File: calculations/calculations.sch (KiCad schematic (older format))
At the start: 24 parts

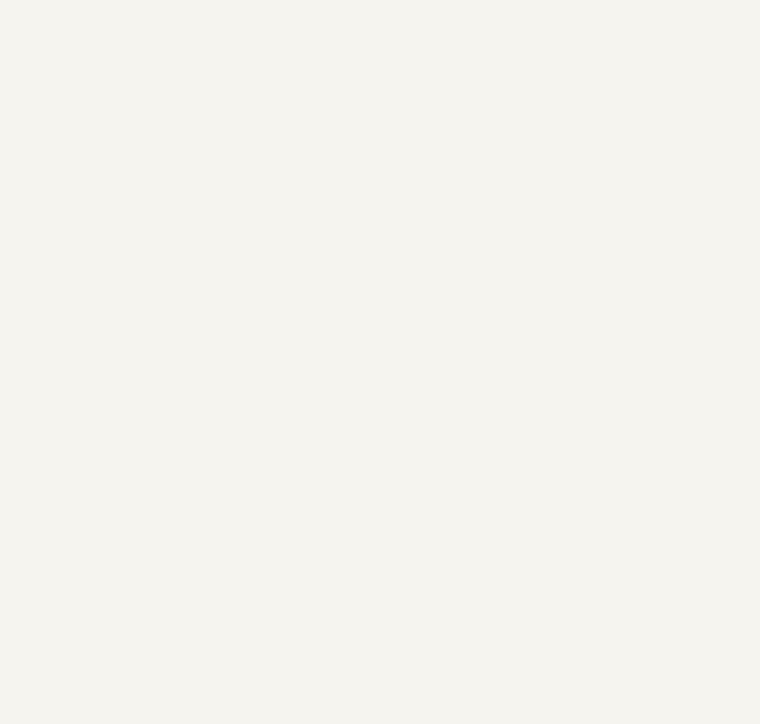
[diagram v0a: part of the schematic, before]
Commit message: Add stage 4 circuit
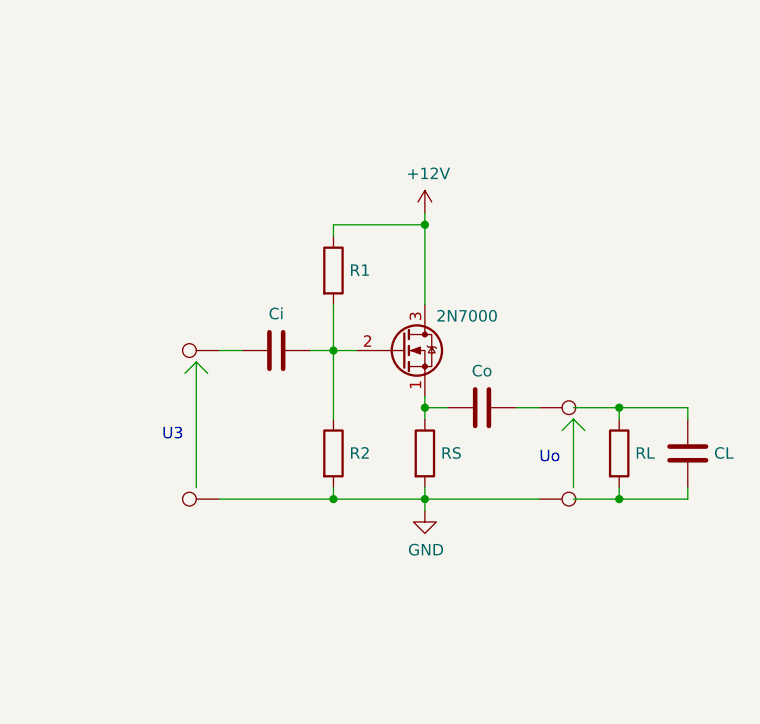
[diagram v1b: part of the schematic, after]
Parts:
- added CL, Ci, Co: C, symbol Device:C
- added Q?: 2N7000, Package_TO_SOT_THT:TO-92_Inline, symbol Transistor_FET:2N7000
- added R1, R2, RL, RS: R, symbol Device:R
- added TP? (x4): TestPoint, symbol Connector:TestPoint
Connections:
- net labels added: +12V
- wire segments 62 -> 95
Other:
- note added: "Uo"
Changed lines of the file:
@@
 Wire Wire Line
 	3750 5950 3700 6000
+$Comp
+L Transistor_FET:2N7000 Q?
+U 1 1 62310B2E
+P 6850 3550
+F 0 "Q?" H 7054 3596 50  0001 L CNN
+F 1 "2N7000" H 7000 3700 50  0000 L CNN
+F 2 "Package_TO_SOT_THT:TO-92_Inline" H 7050 3475 50  0001 L CIN
+F 3 "https://www.onsemi.com/pub/Collateral/NDS7002A-D.PDF" H 6850 3550 50  0001 L CNN
+	1    6850 3550
+	1    0    0    -1
+$EndComp
+$Comp
+L Device:R RS
+U 1 1 623115D3
+P 6950 4000
+F 0 "RS" H 7020 4000 50  0000 L CNN
+F 1 "R" H 7020 3955 50  0001 L CNN
+F 2 "" V 6880 4000 50  0001 C CNN
+F 3 "~" H 6950 4000 50  0001 C CNN
+	1    6950 4000
+	1    0    0    -1
+$EndComp
+$Comp
+L Device:R R2
+U 1 1 62311F48
+P 6550 4000
+F 0 "R2" H 6620 4000 50  0000 L CNN
+F 1 "R" H 6620 3955 50  0001 L CNN
+F 2 "" V 6480 4000 50  0001 C CNN
+F 3 "~" H 6550 4000 50  0001 C CNN
+	1    6550 4000
+	1    0    0    -1
+$EndComp
+$Comp
+L Device:R R1
+U 1 1 62312D4E
+P 6550 3200
+F 0 "R1" H 6620 3200 50  0000 L CNN
+F 1 "R" H 6620 3155 50  0001 L CNN
+F 2 "" V 6480 3200 50  0001 C CNN
+F 3 "~" H 6550 3200 50  0001 C CNN
+	1    6550 3200
+	1    0    0    -1
+$EndComp
+Wire Wire Line
+	6550 3350 6550 3550
+Wire Wire Line
+	6550 3550 6650 3550
+Wire Wire Line
+	6550 3550 6550 3850
+Connection ~ 6550 3550
+Wire Wire Line
+	6950 3850 6950 3800
+Wire Wire Line
+	6550 3050 6550 3000
+Wire Wire Line
+	6950 3000 6950 3350
+$Comp
+L power:+12V #PWR?
+U 1 1 623170D1
+P 6950 2950
+F 0 "#PWR?" H 6950 2800 50  0001 C CNN
+F 1 "+12V" H 6965 3123 50  0000 C CNN
+F 2 "" H 6950 2950 50  0001 C CNN
+F 3 "" H 6950 2950 50  0001 C CNN
+	1    6950 2950
+	1    0    0    -1
+$EndComp
+$Comp
+L power:GND #PWR?
+U 1 1 6231C51E
+P 6950 4250
+F 0 "#PWR?" H 6950 4000 50  0001 C CNN
+F 1 "GND" H 6955 4077 50  0000 C CNN
+F 2 "" H 6950 4250 50  0001 C CNN
+F 3 "" H 6950 4250 50  0001 C CNN
+	1    6950 4250
+	1    0    0    -1
+$EndComp
+Wire Wire Line
+	6950 4150 6950 4200
+Wire Wire Line
+	6550 4150 6550 4200
+Wire Wire Line
+	6550 4200 6950 4200
+Connection ~ 6950 4200
+Wire Wire Line
+	6950 4200 6950 4250
+$Comp
+L Device:C Ci
+U 1 1 6231FE0D
+P 6300 3550
+F 0 "Ci" V 6140 3550 50  0000 C CNN
+F 1 "C" V 6139 3550 50  0001 C CNN
+F 2 "" H 6338 3400 50  0001 C CNN
+F 3 "~" H 6300 3550 50  0001 C CNN
+	1    6300 3550
+	0    1    1    0
+$EndComp
+Wire Wire Line
+	6450 3550 6550 3550
+$Comp
+L Device:C Co
+U 1 1 623245CF
+P 7200 3800
+F 0 "Co" V 7040 3800 50  0000 C CNN
+F 1 "C" V 7039 3800 50  0001 C CNN
+F 2 "" H 7238 3650 50  0001 C CNN
+F 3 "~" H 7200 3800 50  0001 C CNN
+	1    7200 3800
+	0    1    1    0
+$EndComp
+Wire Wire Line
+	6950 3800 7050 3800
+Connection ~ 6950 3800
+Wire Wire Line
+	6950 3800 6950 3750
+$Comp
+L Connector:TestPoint TP?
+U 1 1 62326A7D
+P 7450 3800
+F 0 "TP?" V 7450 3988 50  0001 L CNN
+F 1 "TestPoint" V 7495 3988 50  0001 L CNN
+F 2 "" H 7650 3800 50  0001 C CNN
+F 3 "~" H 7650 3800 50  0001 C CNN
+	1    7450 3800
+	0    1    1    0
+$EndComp
+$Comp
+L Connector:TestPoint TP?
+U 1 1 62327C92
+P 7450 4200
+F 0 "TP?" V 7450 4388 50  0001 L CNN
+F 1 "TestPoint" V 7495 4388 50  0001 L CNN
+F 2 "" H 7650 4200 50  0001 C CNN
+F 3 "~" H 7650 4200 50  0001 C CNN
+	1    7450 4200
+	0    1    1    0
+$EndComp
+$Comp
+L Device:R RL
+U 1 1 6232821D
+P 7800 4000
+F 0 "RL" H 7870 4000 50  0000 L CNN
+F 1 "R" H 7870 3955 50  0001 L CNN
+F 2 "" V 7730 4000 50  0001 C CNN
+F 3 "~" H 7800 4000 50  0001 C CNN
+	1    7800 4000
+	1    0    0    -1
+$EndComp
+Wire Wire Line
+	7800 3850 7800 3800
+Wire Wire Line
+	7800 3800 7600 3800
+Wire Wire Line
+	7800 4150 7800 4200
+Wire Wire Line
+	7800 4200 7600 4200
+Wire Wire Line
+	7450 4200 6950 4200
+Wire Wire Line
+	7450 3800 7350 3800
+$Comp
+L Device:C CL
+U 1 1 6232D62C
+P 8100 4000
+F 0 "CL" H 7985 4000 50  0000 R CNN
+F 1 "C" V 7939 4000 50  0001 C CNN
+F 2 "" H 8138 3850 50  0001 C CNN
+F 3 "~" H 8100 4000 50  0001 C CNN
+	1    8100 4000
+	-1   0    0    1
+$EndComp
+Wire Wire Line
+	7800 3800 8100 3800
+Wire Wire Line
+	8100 3800 8100 3850
+Connection ~ 7800 3800
+Wire Wire Line
+	7800 4200 8100 4200
+Wire Wire Line
+	8100 4200 8100 4150
+Connection ~ 7800 4200
+$Comp
+L Connector:TestPoint TP?
+U 1 1 62331243
+P 6050 3550
+F 0 "TP?" V 6050 3738 50  0001 L CNN
+F 1 "TestPoint" V 6095 3738 50  0001 L CNN
+F 2 "" H 6250 3550 50  0001 C CNN
+F 3 "~" H 6250 3550 50  0001 C CNN
+	1    6050 3550
+	0    -1   -1   0
+$EndComp
+$Comp
+L Connector:TestPoint TP?
+U 1 1 623315B3
+P 6050 4200
+F 0 "TP?" V 6050 4388 50  0001 L CNN
+F 1 "TestPoint" V 6095 4388 50  0001 L CNN
+F 2 "" H 6250 4200 50  0001 C CNN
+F 3 "~" H 6250 4200 50  0001 C CNN
+	1    6050 4200
+	0    -1   -1   0
+$EndComp
+Wire Wire Line
+	6550 4200 6050 4200
+Connection ~ 6550 4200
+Wire Wire Line
+	6050 3550 6150 3550
+Wire Wire Line
+	5950 4150 5950 3600
+Wire Wire Line
+	5950 3600 6000 3650
+Wire Wire Line
+	5950 3600 5900 3650
+Wire Wire Line
+	7600 4150 7600 3850
+Wire Wire Line
+	7600 3850 7650 3900
+Wire Wire Line
+	7600 3850 7550 3900
+Text Notes 5800 3950 0    50   ~ 0
+U3
+Text Notes 7450 4050 0    50   ~ 0
+Uo
+Wire Wire Line
+	6550 3000 6950 3000
+Connection ~ 6950 3000
+Wire Wire Line
+	6950 3000 6950 2950
 $EndSCHEMATC

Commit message: [Calculations] Finish calculations
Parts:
- added CN (x3), CP: C, symbol Device:C
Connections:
- wire segments 95 -> 103
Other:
- moved on the sheet: RF, RN, RP
